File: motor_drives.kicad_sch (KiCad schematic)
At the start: 20 parts, among them U1 DRV8871DDA, U2 DRV8871DDA

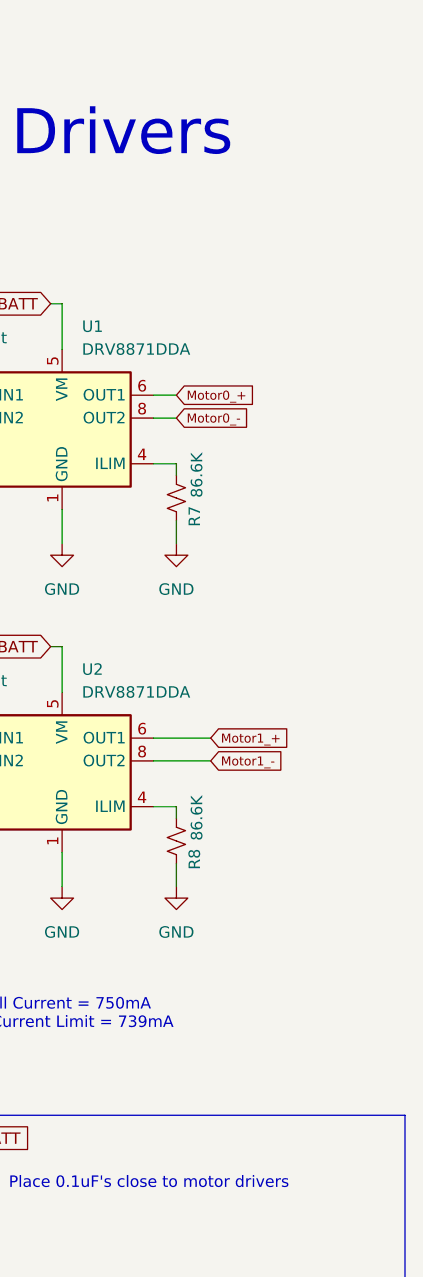
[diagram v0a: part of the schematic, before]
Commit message: Updated schematics
Added the input current sense, expansion header and various test points.
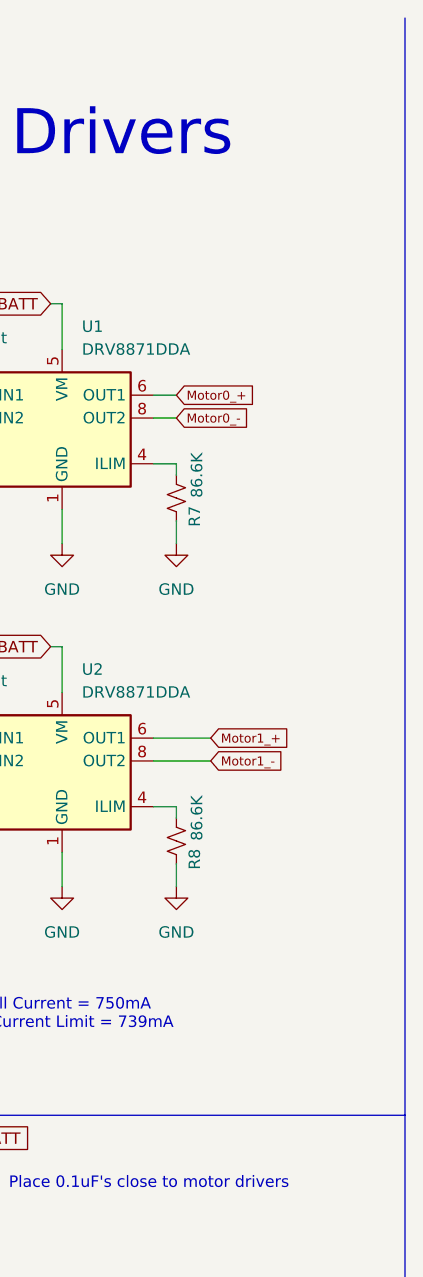
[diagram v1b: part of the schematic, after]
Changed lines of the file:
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@@
+		)
+	)
+	(polyline
+		(pts
+			(xy 86.36 12.7) (xy 86.36 134.62)
+		)
+		(stroke
+			(width 0)
+			(type default)
 		)
 	)

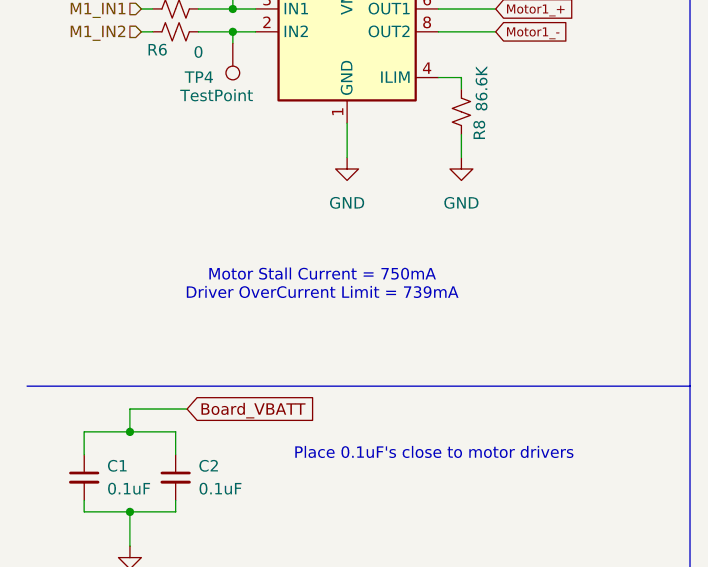
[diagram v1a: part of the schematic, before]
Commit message: Setup top sheet
Added TVS diodes, updated top sheet, misc label fixes
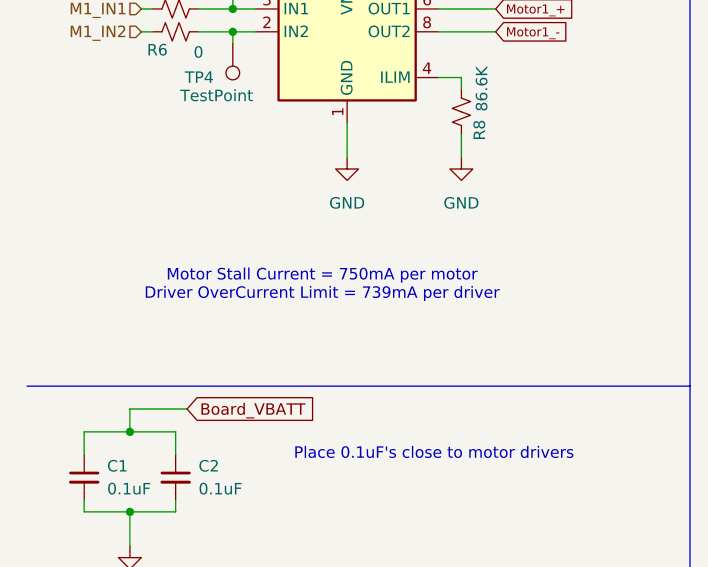
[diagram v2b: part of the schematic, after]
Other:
- note added: "Motor Stall Current = 750mA per motor Driver OverCurrent Limit = 739mA per driver"
- note removed: "Motor Stall Current = 750mA Driver OverCurrent Limit = 739mA"
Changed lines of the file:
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@@
 		)
 	)
-	(text "Motor Stall Current = 750mA\nDriver OverCurrent Limit = 739mA"
+	(text "Motor Stall Current = 750mA per motor\nDriver OverCurrent Limit = 739mA per driver\n"
 		(exclude_from_sim no)
 		(at 45.466 123.444 0)

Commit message: started layout
Preliminary footprint selection
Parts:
- C1, C2: footprint (none) -> Capacitor_SMD:C_0603_1608Metric_Pad1.08x0.95mm_HandSolder
- C3, C4, C5, C6, C7, C8: footprint (none) -> Capacitor_SMD:C_0805_2012Metric_Pad1.18x1.45mm_HandSolder
- R3, R4, R5, R6, R7, R8: footprint (none) -> Resistor_SMD:R_0603_1608Metric
- TP1, TP2, TP3, TP4: footprint (none) -> TestPoint:TestPoint_Pad_1.0x1.0mm
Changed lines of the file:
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@@
 			)
 		)
-		(property "Footprint" ""
+		(property "Footprint" "Capacitor_SMD:C_0805_2012Metric_Pad1.18x1.45mm_HandSolder"
 			(at 64.77 175.26 0)
 			(effects
@@
 			)
 		)
-		(property "Footprint" ""
+		(property "Footprint" "Resistor_SMD:R_0603_1608Metric"
 			(at 60.96 104.14 0)
 			(effects
@@
 			)
 		)
-		(property "Footprint" ""
+		(property "Footprint" "Capacitor_SMD:C_0805_2012Metric_Pad1.18x1.45mm_HandSolder"
 			(at 22.86 175.26 0)
 			(effects
@@
 			)
 		)
-		(property "Footprint" ""
+		(property "Footprint" "Capacitor_SMD:C_0805_2012Metric_Pad1.18x1.45mm_HandSolder"
 			(at 43.18 175.26 0)
 			(effects
@@
 			)
 		)
-		(property "Footprint" ""
+		(property "Footprint" "TestPoint:TestPoint_Pad_1.0x1.0mm"
 			(at 40.64 91.44 0)
 			(effects
@@
 			)
 		)
-		(property "Footprint" ""
+		(property "Footprint" "Resistor_SMD:R_0603_1608Metric"
 			(at 60.96 66.04 0)
 			(effects
@@
 			)
 		)
-		(property "Footprint" ""
+		(property "Footprint" "Resistor_SMD:R_0603_1608Metric"
 			(at 29.21 54.61 0)
 			(effects
@@
 			)
 		)
-		(property "Footprint" ""
+		(property "Footprint" "Capacitor_SMD:C_0805_2012Metric_Pad1.18x1.45mm_HandSolder"
 			(at 33.02 175.26 0)
 			(effects
@@
 			)
 		)
-		(property "Footprint" ""
+		(property "Footprint" "TestPoint:TestPoint_Pad_1.0x1.0mm"
 			(at 30.48 96.52 0)
 			(effects
@@
 			)
 		)
-		(property "Footprint" ""
+		(property "Footprint" "Resistor_SMD:R_0603_1608Metric"
 			(at 29.21 57.15 0)
 			(effects
@@
 			)
 		)
-		(property "Footprint" ""
+		(property "Footprint" "TestPoint:TestPoint_Pad_1.0x1.0mm"
 			(at 40.64 53.34 0)
 			(effects
@@
 			)
 		)
-		(property "Footprint" ""
+		(property "Footprint" "Capacitor_SMD:C_0603_1608Metric_Pad1.08x0.95mm_HandSolder"
 			(at 19.05 144.78 0)
 			(effects
@@
 			)
 		)
-		(property "Footprint" ""
+		(property "Footprint" "TestPoint:TestPoint_Pad_1.0x1.0mm"
 			(at 30.48 58.42 0)
 			(effects
@@
 			)
 		)
-		(property "Footprint" ""
+		(property "Footprint" "Capacitor_SMD:C_0603_1608Metric_Pad1.08x0.95mm_HandSolder"
 			(at 29.21 144.78 0)
 			(effects
@@
 			)
 		)
-		(property "Footprint" ""
+		(property "Footprint" "Resistor_SMD:R_0603_1608Metric"
 			(at 29.21 92.71 0)
 			(effects
@@
 			)
 		)
-		(property "Footprint" ""
+		(property "Footprint" "Capacitor_SMD:C_0805_2012Metric_Pad1.18x1.45mm_HandSolder"
 			(at 74.93 175.26 0)
 			(effects
@@
 			)
 		)
-		(property "Footprint" ""
+		(property "Footprint" "Resistor_SMD:R_0603_1608Metric"
 			(at 29.21 95.25 0)
 			(effects
@@
 			)
 		)
-		(property "Footprint" ""
+		(property "Footprint" "Capacitor_SMD:C_0805_2012Metric_Pad1.18x1.45mm_HandSolder"
 			(at 53.34 175.26 0)
 			(effects

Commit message: footprint cleanup
switched to 0402 resistors, updated connectors, etc...
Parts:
- R3, R4, R5, R6, R7, R8: footprint Resistor_SMD:R_0603_1608Metric -> Resistor_SMD:R_0402_1005Metric
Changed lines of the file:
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@@
 			)
 		)
-		(property "Footprint" "Resistor_SMD:R_0603_1608Metric"
+		(property "Footprint" "Resistor_SMD:R_0402_1005Metric"
 			(at 60.96 104.14 0)
 			(effects
@@
 			)
 		)
-		(property "Footprint" "Resistor_SMD:R_0603_1608Metric"
+		(property "Footprint" "Resistor_SMD:R_0402_1005Metric"
 			(at 60.96 66.04 0)
 			(effects
@@
 			)
 		)
-		(property "Footprint" "Resistor_SMD:R_0603_1608Metric"
+		(property "Footprint" "Resistor_SMD:R_0402_1005Metric"
 			(at 29.21 54.61 0)
 			(effects
@@
 			)
 		)
-		(property "Footprint" "Resistor_SMD:R_0603_1608Metric"
+		(property "Footprint" "Resistor_SMD:R_0402_1005Metric"
 			(at 29.21 57.15 0)
 			(effects
@@
 			)
 		)
-		(property "Footprint" "Resistor_SMD:R_0603_1608Metric"
+		(property "Footprint" "Resistor_SMD:R_0402_1005Metric"
 			(at 29.21 92.71 0)
 			(effects
@@
 			)
 		)
-		(property "Footprint" "Resistor_SMD:R_0603_1608Metric"
+		(property "Footprint" "Resistor_SMD:R_0402_1005Metric"
 			(at 29.21 95.25 0)
 			(effects

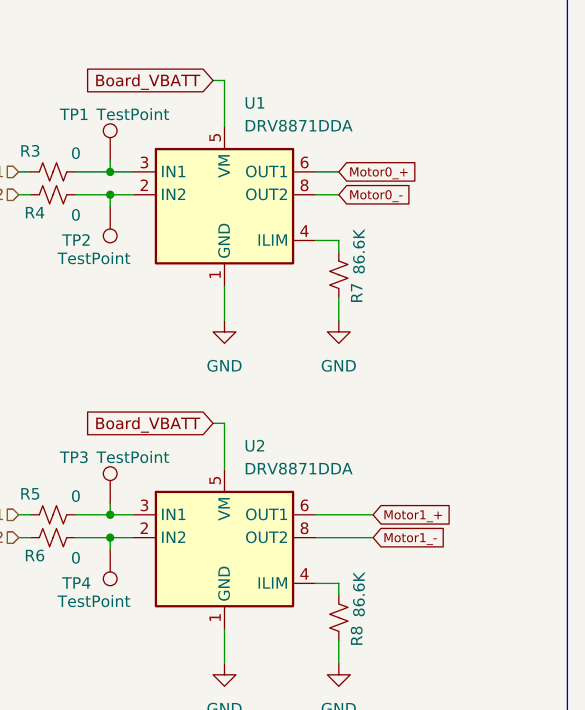
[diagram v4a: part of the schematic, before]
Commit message: Swapped motor polarity
Swapped motor polarity for easier routing + other component positioning.
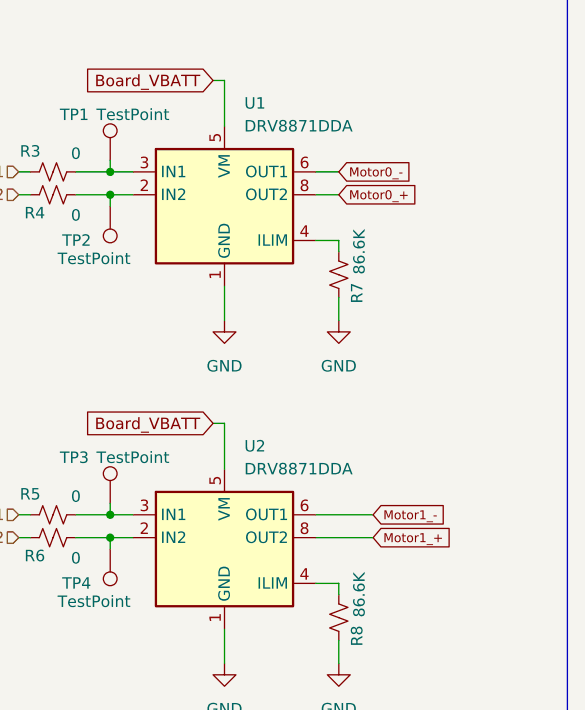
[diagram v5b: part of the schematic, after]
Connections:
- net Motor0_+: now also U1.8 (OUT2); no longer U1.6 (OUT1)
- net Motor0_-: now also U1.6 (OUT1); no longer U1.8 (OUT2)
- net Motor1_+: now also U2.8 (OUT2); no longer U2.6 (OUT1)
- net Motor1_-: now also U2.6 (OUT1); no longer U2.8 (OUT2)
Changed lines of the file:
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@@
 	(global_label "Motor1_-"
 		(shape input)
-		(at 64.77 95.25 0)
+		(at 64.77 92.71 0)
 		(fields_autoplaced yes)
 		(effects
@@
 		)
 		(property "Intersheetrefs" "${INTERSHEET_REFS}"
-			(at 74.2156 95.25 0)
+			(at 74.2156 92.71 0)
 			(effects
 				(font
@@
 	(global_label "Motor0_+"
 		(shape input)
-		(at 60.96 54.61 0)
+		(at 60.96 57.15 0)
 		(fields_autoplaced yes)
 		(effects
@@
 		)
 		(property "Intersheetrefs" "${INTERSHEET_REFS}"
-			(at 70.4056 54.61 0)
+			(at 70.4056 57.15 0)
 			(effects
 				(font
@@
 	(global_label "Motor0_-"
 		(shape input)
-		(at 60.96 57.15 0)
+		(at 60.96 54.61 0)
 		(fields_autoplaced yes)
 		(effects
@@
 		)
 		(property "Intersheetrefs" "${INTERSHEET_REFS}"
-			(at 70.4056 57.15 0)
+			(at 70.4056 54.61 0)
 			(effects
 				(font
@@
 	(global_label "Motor1_+"
 		(shape input)
-		(at 64.77 92.71 0)
+		(at 64.77 95.25 0)
 		(fields_autoplaced yes)
 		(effects
@@
 		)
 		(property "Intersheetrefs" "${INTERSHEET_REFS}"
-			(at 74.2156 92.71 0)
+			(at 74.2156 95.25 0)
 			(effects
 				(font

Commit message: Layout updates
testpoints, usb power, etc.
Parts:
- TP1, TP2, TP3, TP4: footprint TestPoint:TestPoint_Pad_1.0x1.0mm -> TestPoint:TestPoint_Pad_D1.0mm
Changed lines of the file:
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@@
 			)
 		)
-		(property "Footprint" "TestPoint:TestPoint_Pad_1.0x1.0mm"
+		(property "Footprint" "TestPoint:TestPoint_Pad_D1.0mm"
 			(at 40.64 91.44 0)
 			(effects
@@
 			)
 		)
-		(property "Footprint" "TestPoint:TestPoint_Pad_1.0x1.0mm"
+		(property "Footprint" "TestPoint:TestPoint_Pad_D1.0mm"
 			(at 30.48 96.52 0)
 			(effects
@@
 			)
 		)
-		(property "Footprint" "TestPoint:TestPoint_Pad_1.0x1.0mm"
+		(property "Footprint" "TestPoint:TestPoint_Pad_D1.0mm"
 			(at 40.64 53.34 0)
 			(effects
@@
 			)
 		)
-		(property "Footprint" "TestPoint:TestPoint_Pad_1.0x1.0mm"
+		(property "Footprint" "TestPoint:TestPoint_Pad_D1.0mm"
 			(at 30.48 58.42 0)
 			(effects

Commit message: Bom updates
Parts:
- C1, C2: MPN (none) -> CC0603KRX7R7BB104; Package (none) -> 0603
- C3, C4, C5, C6, C7, C8: MPN (none) -> CL21A106KOQNNNE; Package (none) -> 0805
- R3, R4, R5, R6: MPN (none) -> RC0402FR-070RL; Package (none) -> 0402
- R7, R8: MPN (none) -> CRCW040286K6FKEDC; Package (none) -> 0402
- TP1, TP2, TP3, TP4: now not fitted
- U1, U2: MPN (none) -> DRV8871DDAR; Package (none) -> 8-PowerSOIC (0.154", 3.90mm Width)
